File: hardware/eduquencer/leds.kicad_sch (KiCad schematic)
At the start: 18 parts

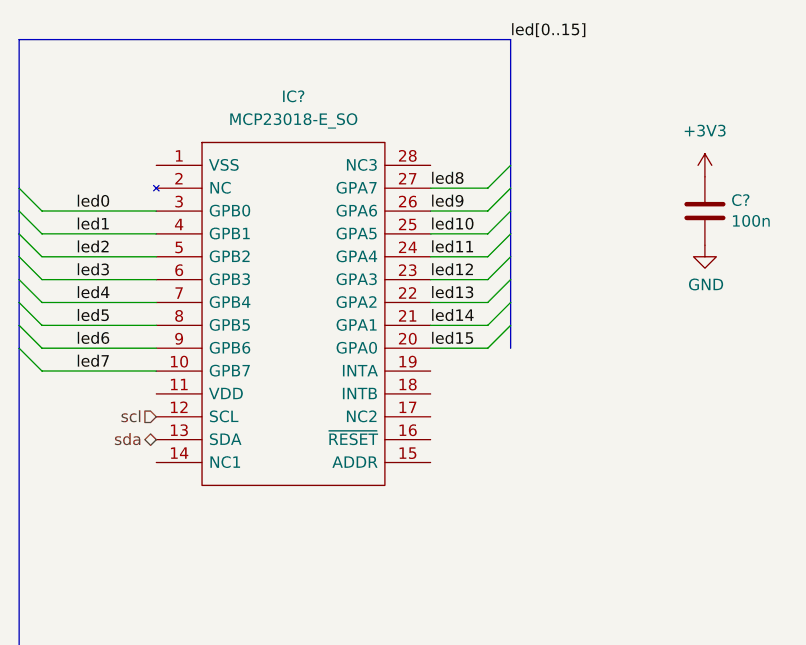
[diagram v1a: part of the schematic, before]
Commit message: Hardware: LEDs schematics adjustments
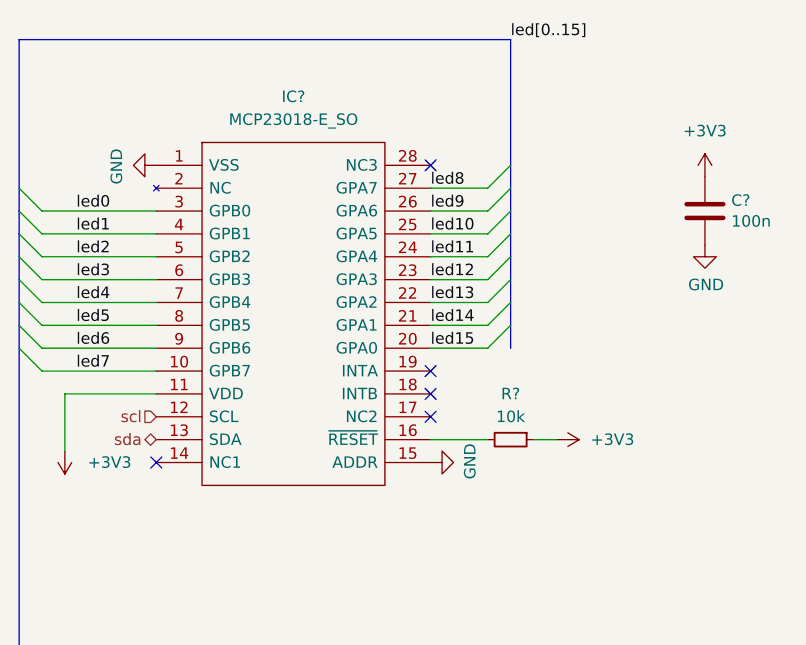
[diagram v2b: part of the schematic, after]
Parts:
- added R?: 10k, symbol Device:R_Small
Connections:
- net +3V3: now also IC?.11 (VDD), R?.1
- net GND: now also IC?.1 (VSS), IC?.15 (ADDR)
- net at IC?.16 (~{RESET}): now also R?.2
- no-connect marks 0 -> 5
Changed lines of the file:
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@@
 (kicad_sch (version 20211123) (generator eeschema)
   (paper "A4")
+  (no_connect (at 85.09 40.64))
+  (no_connect (at 54.61 73.66))
+  (no_connect (at 85.09 68.58))
+  (no_connect (at 85.09 63.5))
+  (no_connect (at 85.09 66.04))
   (bus_entry (at 91.44 58.42) (size 2.54 -2.54)
     (stroke (width 0) (type default) (color 0 0 0 0))
@@
     (stroke (width 0) (type default) (color 0 0 0 0))
   )
+  (wire (pts (xy 85.09 71.12) (xy 91.44 71.12))
+    (stroke (width 0) (type default) (color 0 0 0 0))
+  )
   (wire (pts (xy 210.82 109.22) (xy 210.82 111.76))
     (stroke (width 0) (type default) (color 0 0 0 0))
@@
     (stroke (width 0) (type default) (color 0 0 0 0))
   )
+  (wire (pts (xy 44.45 66.04) (xy 54.61 66.04))
+    (stroke (width 0) (type default) (color 0 0 0 0))
+  )
   (wire (pts (xy 154.94 139.7) (xy 154.94 143.51))
     (stroke (width 0) (type default) (color 0 0 0 0))
@@
     (stroke (width 0) (type default) (color 0 0 0 0))
   )
+  (wire (pts (xy 44.45 72.39) (xy 44.45 66.04))
+    (stroke (width 0) (type default) (color 0 0 0 0))
+  )
   (bus (pts (xy 208.28 106.68) (xy 234.95 106.68))
     (stroke (width 0) (type default) (color 0 0 0 0))
@@
   )
   (wire (pts (xy 127 109.22) (xy 127 111.76))
+    (stroke (width 0) (type default) (color 0 0 0 0))
+  )
+  (wire (pts (xy 96.52 71.12) (xy 99.06 71.12))
     (stroke (width 0) (type default) (color 0 0 0 0))
   )
@@
   (hierarchical_label "sda" (shape bidirectional) (at 54.61 71.12 180)
     (effects (font (size 1.27 1.27)) (justify right))
+  )
+  (symbol (lib_id "Device:R_Small") (at 93.98 71.12 270) (unit 1)
+    (in_bom yes) (on_board yes)
+    (property "Reference" "R?" (id 0) (at 93.98 66.04 90))
+    (property "Value" "10k" (id 1) (at 93.98 68.58 90))
+    (property "Footprint" "" (id 2) (at 93.98 71.12 0)
+      (effects (font (size 1.27 1.27)) hide)
+    )
+    (property "Datasheet" "~" (id 3) (at 93.98 71.12 0)
+      (effects (font (size 1.27 1.27)) hide)
+    )
+    (pin "1")
+    (pin "2")
   )
   (symbol (lib_id "XZMYK45WT-9:XZMYK45WT-9") (at 237.49 127 90) (unit 1)
@@
     (pin "2")
   )
+  (symbol (lib_id "power:GND") (at 54.61 40.64 270) (unit 1)
+    (in_bom yes) (on_board yes)
+    (property "Reference" "#PWR?" (id 0) (at 48.26 40.64 0)
+      (effects (font (size 1.27 1.27)) hide)
+    )
+    (property "Value" "GND" (id 1) (at 50.2158 40.767 0))
+    (property "Footprint" "" (id 2) (at 54.61 40.64 0)
+      (effects (font (size 1.27 1.27)) hide)
+    )
+    (property "Datasheet" "" (id 3) (at 54.61 40.64 0)
+      (effects (font (size 1.27 1.27)) hide)
+    )
+    (pin "1")
+  )
   (symbol (lib_id "Device:C") (at 115.57 45.72 0) (unit 1)
     (in_bom yes) (on_board yes)
@@
     (pin "2")
   )
+  (symbol (lib_id "power:GND") (at 85.09 73.66 90) (unit 1)
+    (in_bom yes) (on_board yes)
+    (property "Reference" "#PWR?" (id 0) (at 91.44 73.66 0)
+      (effects (font (size 1.27 1.27)) hide)
+    )
+    (property "Value" "GND" (id 1) (at 89.4842 73.533 0))
+    (property "Footprint" "" (id 2) (at 85.09 73.66 0)
+      (effects (font (size 1.27 1.27)) hide)
+    )
+    (property "Datasheet" "" (id 3) (at 85.09 73.66 0)
+      (effects (font (size 1.27 1.27)) hide)
+    )
+    (pin "1")
+  )
+  (symbol (lib_id "power:+3V3") (at 99.06 71.12 270) (unit 1)
+    (in_bom yes) (on_board yes) (fields_autoplaced)
+    (property "Reference" "#PWR?" (id 0) (at 95.25 71.12 0)
+      (effects (font (size 1.27 1.27)) hide)
+    )
+    (property "Value" "+3V3" (id 1) (at 102.87 71.1199 90)
+      (effects (font (size 1.27 1.27)) (justify left))
+    )
+    (property "Footprint" "" (id 2) (at 99.06 71.12 0)
+      (effects (font (size 1.27 1.27)) hide)
+    )
+    (property "Datasheet" "" (id 3) (at 99.06 71.12 0)
+      (effects (font (size 1.27 1.27)) hide)
+    )
+    (pin "1")
+  )
+  (symbol (lib_id "power:+3V3") (at 44.45 72.39 180) (unit 1)
+    (in_bom yes) (on_board yes) (fields_autoplaced)
+    (property "Reference" "#PWR?" (id 0) (at 44.45 68.58 0)
+      (effects (font (size 1.27 1.27)) hide)
+    )
+    (property "Value" "+3V3" (id 1) (at 46.99 73.6599 0)
+      (effects (font (size 1.27 1.27)) (justify right))
+    )
+    (property "Footprint" "" (id 2) (at 44.45 72.39 0)
+      (effects (font (size 1.27 1.27)) hide)
+    )
+    (property "Datasheet" "" (id 3) (at 44.45 72.39 0)
+      (effects (font (size 1.27 1.27)) hide)
+    )
+    (pin "1")
+  )
   (symbol (lib_id "XZMYK45WT-9:XZMYK45WT-9") (at 44.45 127 90) (unit 1)

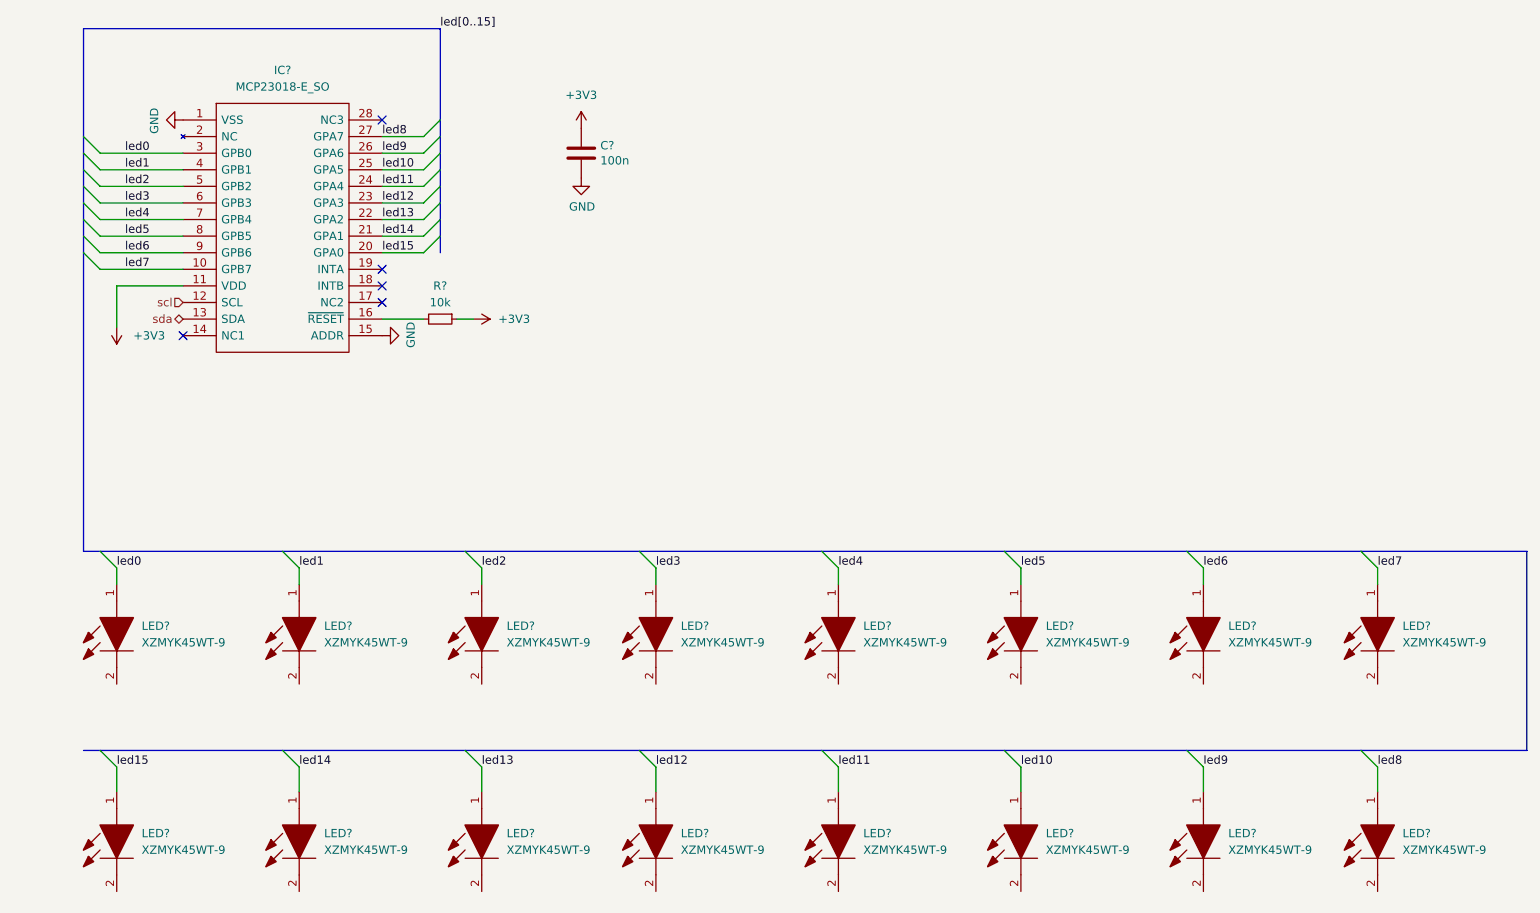
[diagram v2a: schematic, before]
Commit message: Hardware: add button sheet
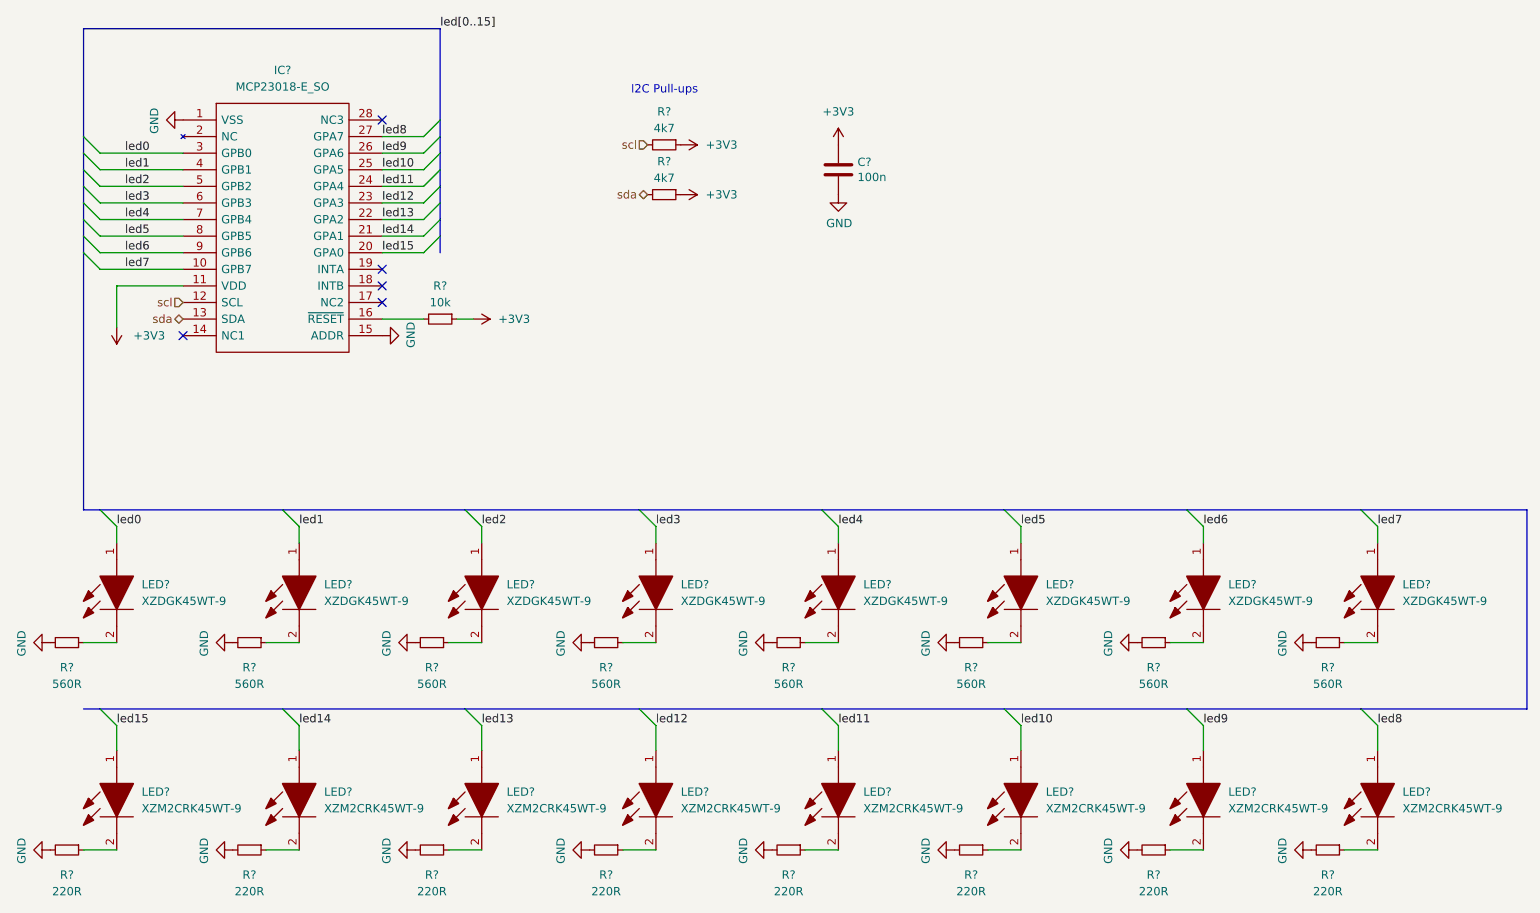
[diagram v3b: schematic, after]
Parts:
- added R? (x8): 560R, symbol Device:R_Small
- added R? (x8): 220R, symbol Device:R_Small
- added R? (x2): 4k7, symbol Device:R_Small
- LED? (x8): value XZMYK45WT-9 -> XZDGK45WT-9
- LED? (x8): value XZMYK45WT-9 -> XZM2CRK45WT-9
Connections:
- net +3V3: now also R?.1, R?.1
- net GND: now also R?.2, R?.2, R?.2, R?.2, R?.2, R?.2, R?.2, R?.2, R?.2, R?.2, R?.2, R?.2, R?.2, R?.2, R?.2, R?.2
- net scl: now also R?.2
- net sda: now also R?.2
- net at LED?.2: now also R?.1 (x16)
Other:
- note added: "I2C Pull-ups"
- moved on the sheet: C?, LED?

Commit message: Hardware: add test points, tiny cleanup
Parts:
- C?: LCSC C14663 -> (none); LCSC Part # C14663 -> (none)

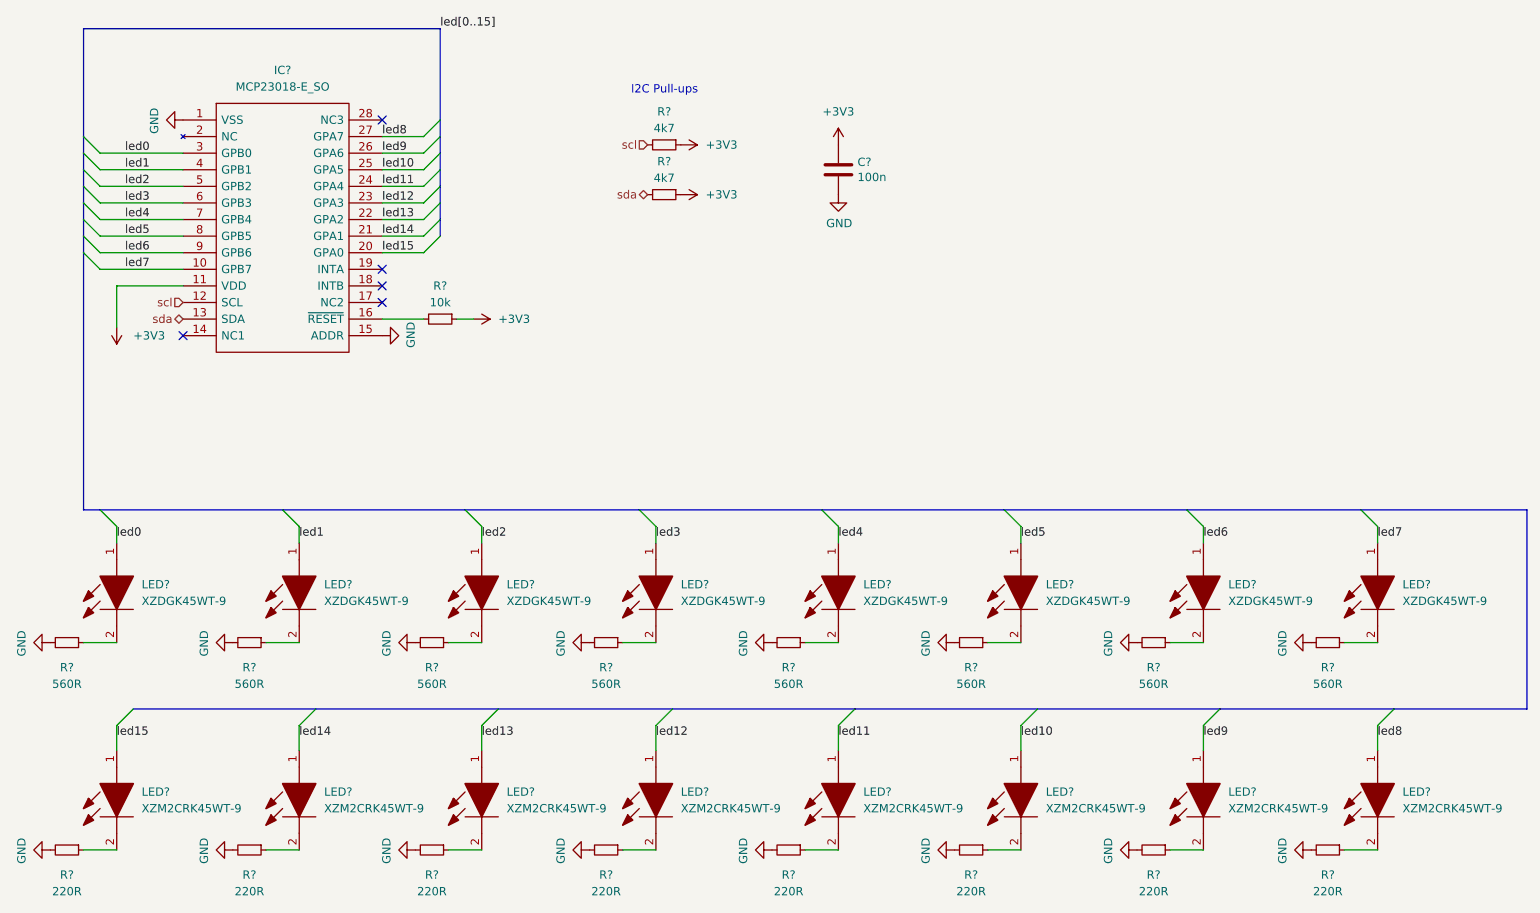
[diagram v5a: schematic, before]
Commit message: Hardware: update models, annotate, fix ERC issues
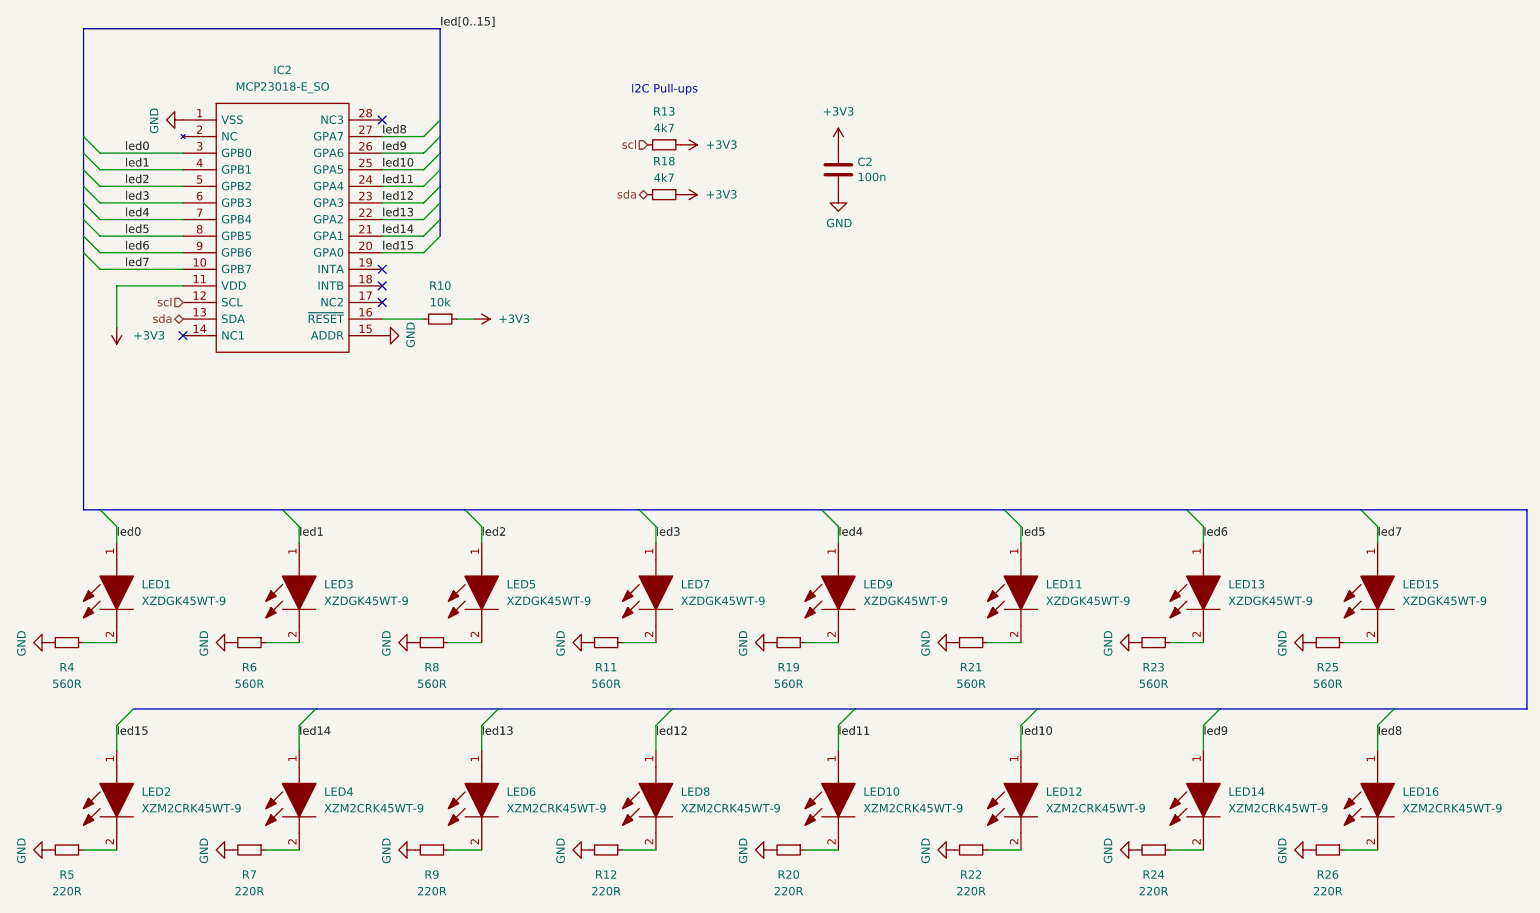
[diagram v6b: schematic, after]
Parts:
- gave numbers to parts that had none: 37

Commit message: Hardware: assign all footprints
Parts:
- C2: footprint Capacitor_SMD:C_0603_1608Metric -> Capacitor_SMD:C_0603_1608Metric_Pad1.08x0.95mm_HandSolder
- IC2: footprint SOIC127P1030X265-28N -> MCP23018-E_SO:SOIC127P1030X265-28N
- LED1, LED10, LED11, LED12, LED13, LED14, LED15, LED16, LED2, LED3, LED4, LED5, LED6, LED7, LED8, LED9: footprint XZMYK45WT9 -> XZMYK45WT-9:XZMYK45WT9
- R10, R11, R12, R13, R18, R19, R20, R21, R22, R23, R24, R25, R26, R4, R5, R6, R7, R8, R9: footprint (none) -> Resistor_SMD:R_0603_1608Metric_Pad0.98x0.95mm_HandSolder
